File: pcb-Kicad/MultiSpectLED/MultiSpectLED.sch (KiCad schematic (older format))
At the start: 102 parts, among them J1 Conn_01x02_Female, J2 USB_C_Receptacle_USB2.0, SW1 NKK_HEXADEC, SW2 NKK_HEXADEC, U1 PAM2804, U10 PAM2804, U11 PAM2804, U12 PAM2804, U13 PAM2804, U14 PAM2804, U15 PAM2804, U16 PAM2804, U2 TeensyLC, U3 PAM2804, U4 PAM2804, U5 PAM2804, U6 PAM2804, U7 PAM2804, U8 PAM2804, U9 PAM2804

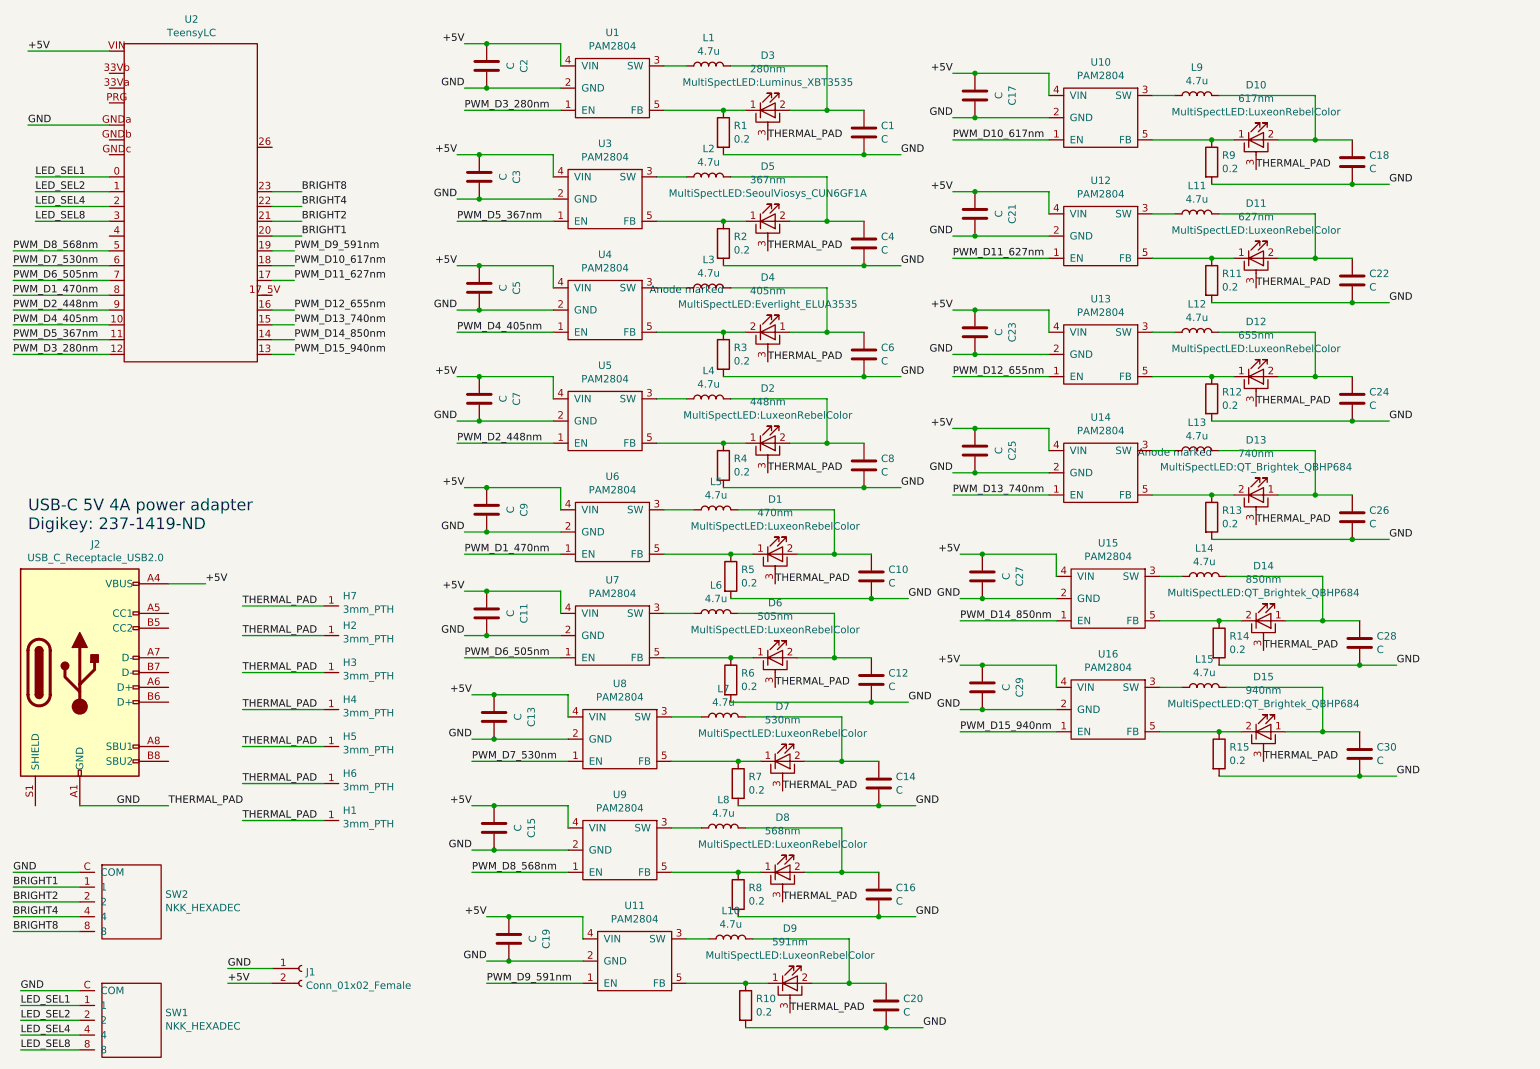
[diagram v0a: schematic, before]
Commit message: Added pulldown resistors on each PAM2804 enable line
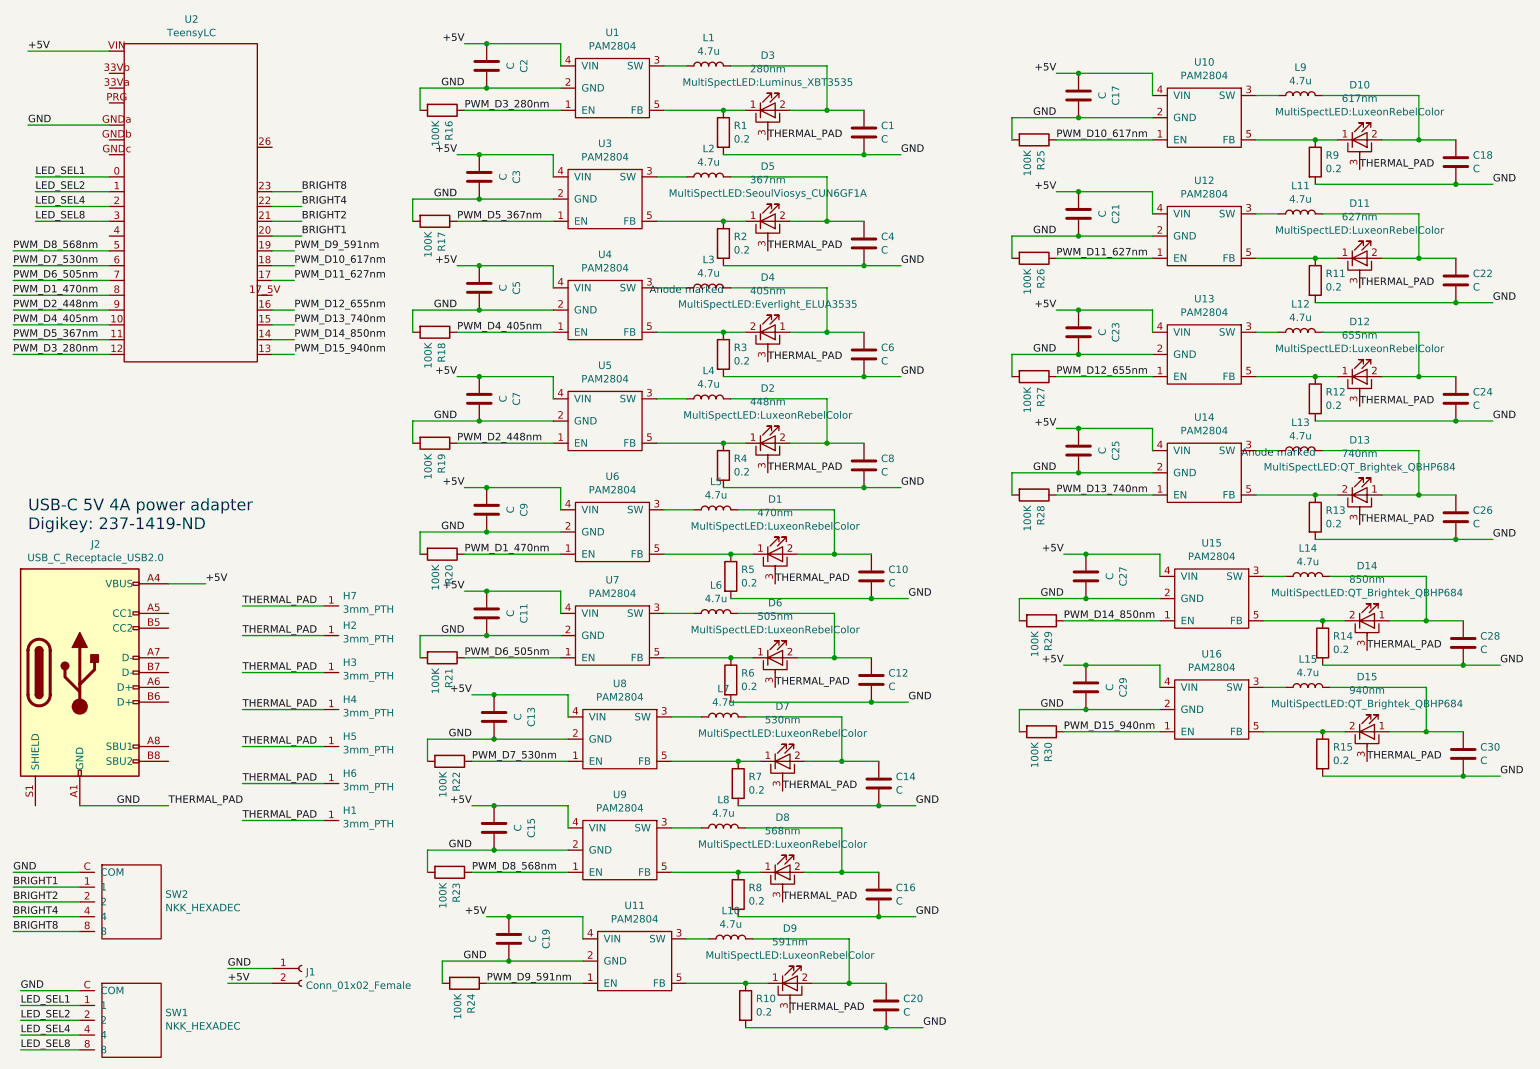
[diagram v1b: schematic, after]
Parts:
- added R16, R17, R18, R19, R20, R21, R22, R23, R24, R25, R26, R27, R28, R29, R30: 100K, MultiSpectLED:R_0402_1005Metric, symbol MultiSpectLED:R
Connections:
- net GND: now also R16.2, R17.2, R18.2, R19.2, R20.2, R21.2, R22.2, R23.2, R24.2, R25.2, R26.2, R27.2, R28.2, R29.2, R30.2
- net PWM_D10_617nm: now also R25.1
- net PWM_D11_627nm: now also R26.1
- net PWM_D12_655nm: now also R27.1
- net PWM_D13_740nm: now also R28.1
- net PWM_D14_850nm: now also R29.1
- net PWM_D15_940nm: now also R30.1
- net PWM_D1_470nm: now also R20.1
- net PWM_D2_448nm: now also R19.1
- net PWM_D3_280nm: now also R16.1
- net PWM_D4_405nm: now also R18.1
- net PWM_D5_367nm: now also R17.1
- net PWM_D6_505nm: now also R21.1
- net PWM_D7_530nm: now also R22.1
- net PWM_D8_568nm: now also R23.1
- net PWM_D9_591nm: now also R24.1
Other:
- moved on the sheet: C17, C18, C21, C22, C23, C24, C25, C26, C27, C28, C29, C30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
